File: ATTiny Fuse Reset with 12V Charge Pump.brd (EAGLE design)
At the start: 59 parts, among them IC1 74HC04D, Q1 BSS138, Q2 PMV65XP, Q3 BSS138, Q4 BSS138, Q5 BSS138, Q6 BSS138, Q7 BSS138, Q8 BSS130, SW3 SWITCH_SPDT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

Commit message: added dimnsion layer
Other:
- board outline added: 68.6 x 53.3 mm
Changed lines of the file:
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@@
 <grid distance="50" unitdist="mil" unit="mil" style="lines" multiple="5" display="yes" altdistance="5" altunitdist="mil" altunit="mil"/>
 <layers>
-<layer number="1" name="Top" color="4" fill="1" visible="yes" active="yes"/>
+<layer number="1" name="Top" color="4" fill="1" visible="no" active="yes"/>
 <layer number="16" name="Bottom" color="1" fill="1" visible="yes" active="yes"/>
-<layer number="17" name="Pads" color="2" fill="1" visible="yes" active="yes"/>
-<layer number="18" name="Vias" color="2" fill="1" visible="yes" active="yes"/>
-<layer number="19" name="Unrouted" color="6" fill="1" visible="yes" active="yes"/>
+<layer number="17" name="Pads" color="2" fill="1" visible="no" active="yes"/>
+<layer number="18" name="Vias" color="2" fill="1" visible="no" active="yes"/>
+<layer number="19" name="Unrouted" color="6" fill="1" visible="no" active="yes"/>
 <layer number="20" name="Dimension" color="15" fill="1" visible="yes" active="yes"/>
-<layer number="21" name="tPlace" color="16" fill="1" visible="yes" active="yes"/>
+<layer number="21" name="tPlace" color="16" fill="1" visible="no" active="yes"/>
 <layer number="22" name="bPlace" color="14" fill="1" visible="yes" active="yes"/>
-<layer number="23" name="tOrigins" color="15" fill="1" visible="yes" active="yes"/>
-<layer number="24" name="bOrigins" color="15" fill="1" visible="yes" active="yes"/>
+<layer number="23" name="tOrigins" color="15" fill="1" visible="no" active="yes"/>
+<layer number="24" name="bOrigins" color="15" fill="1" visible="no" active="yes"/>
 <layer number="25" name="tNames" color="7" fill="1" visible="no" active="yes"/>
 <layer number="26" name="bNames" color="7" fill="1" visible="no" active="yes"/>
@@
 <layer number="32" name="bCream" color="7" fill="5" visible="no" active="yes"/>
 <layer number="44" name="Drills" color="7" fill="1" visible="no" active="yes"/>
-<layer number="45" name="Holes" color="7" fill="1" visible="yes" active="yes"/>
+<layer number="45" name="Holes" color="7" fill="1" visible="no" active="yes"/>
 <layer number="50" name="dxf" color="7" fill="1" visible="no" active="no"/>
-<layer number="51" name="tDocu" color="6" fill="1" visible="yes" active="yes"/>
+<layer number="51" name="tDocu" color="6" fill="1" visible="no" active="yes"/>
 <layer number="52" name="bDocu" color="7" fill="1" visible="no" active="yes"/>
 <layer number="53" name="tGND_GNDA" color="7" fill="9" visible="no" active="no"/>
@@
 HV / ISP
 Programmer</text>
+<wire x1="0" y1="53.34" x2="0" y2="0" width="0.000253125" layer="20"/>
+<wire x1="0" y1="0" x2="66.04" y2="0" width="0.000253125" layer="20"/>
+<wire x1="66.04" y1="0" x2="66.04" y2="2.54" width="0.000253125" layer="20"/>
+<wire x1="66.04" y1="2.54" x2="68.58" y2="5.08" width="0.000253125" layer="20"/>
+<wire x1="68.58" y1="5.08" x2="68.58" y2="37.846" width="0.000253125" layer="20"/>
+<wire x1="68.58" y1="37.846" x2="66.04" y2="40.386" width="0.000253125" layer="20"/>
+<wire x1="66.04" y1="40.386" x2="66.04" y2="51.816" width="0.000253125" layer="20"/>
+<wire x1="66.04" y1="51.816" x2="64.516" y2="53.34" width="0.000253125" layer="20"/>
+<wire x1="64.516" y1="53.34" x2="0" y2="53.34" width="0.000253125" layer="20"/>
 </plain>
 <attributes>

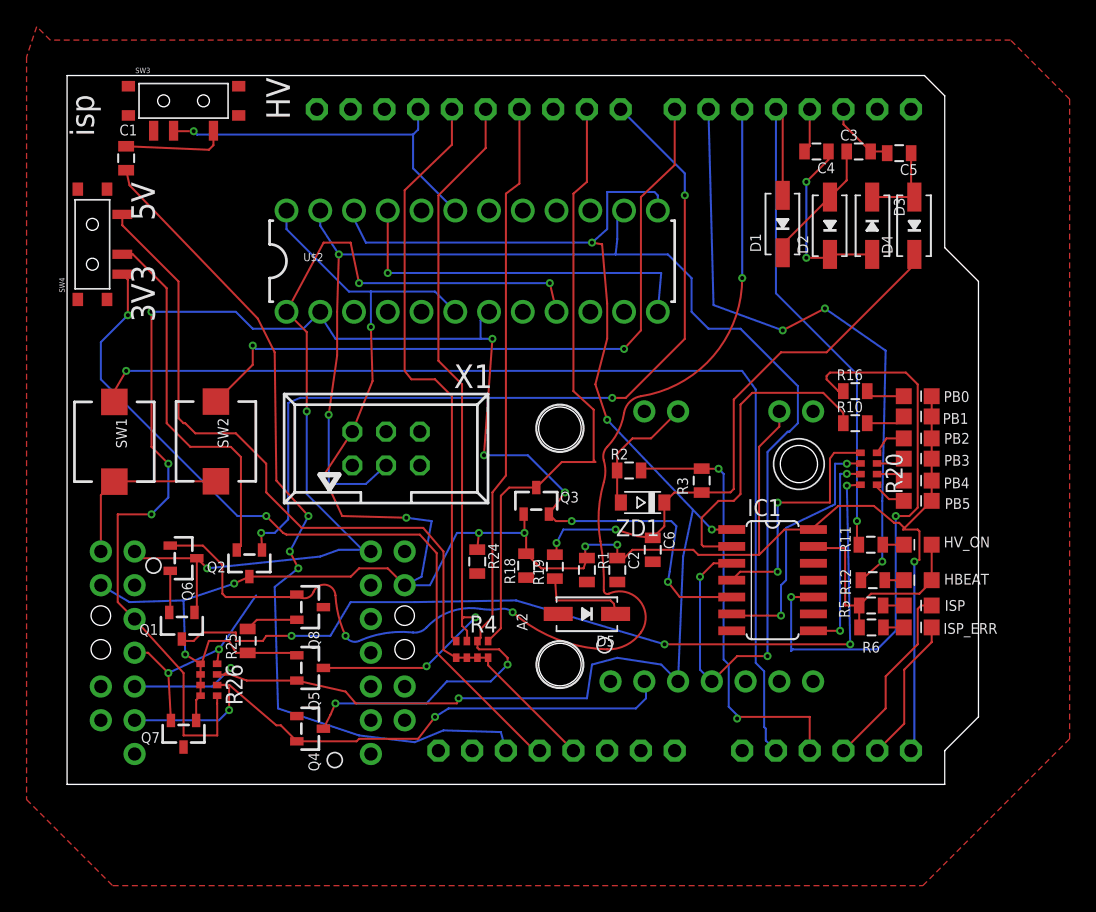
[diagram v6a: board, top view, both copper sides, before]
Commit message: aligned xtra pins overlayed on attami device
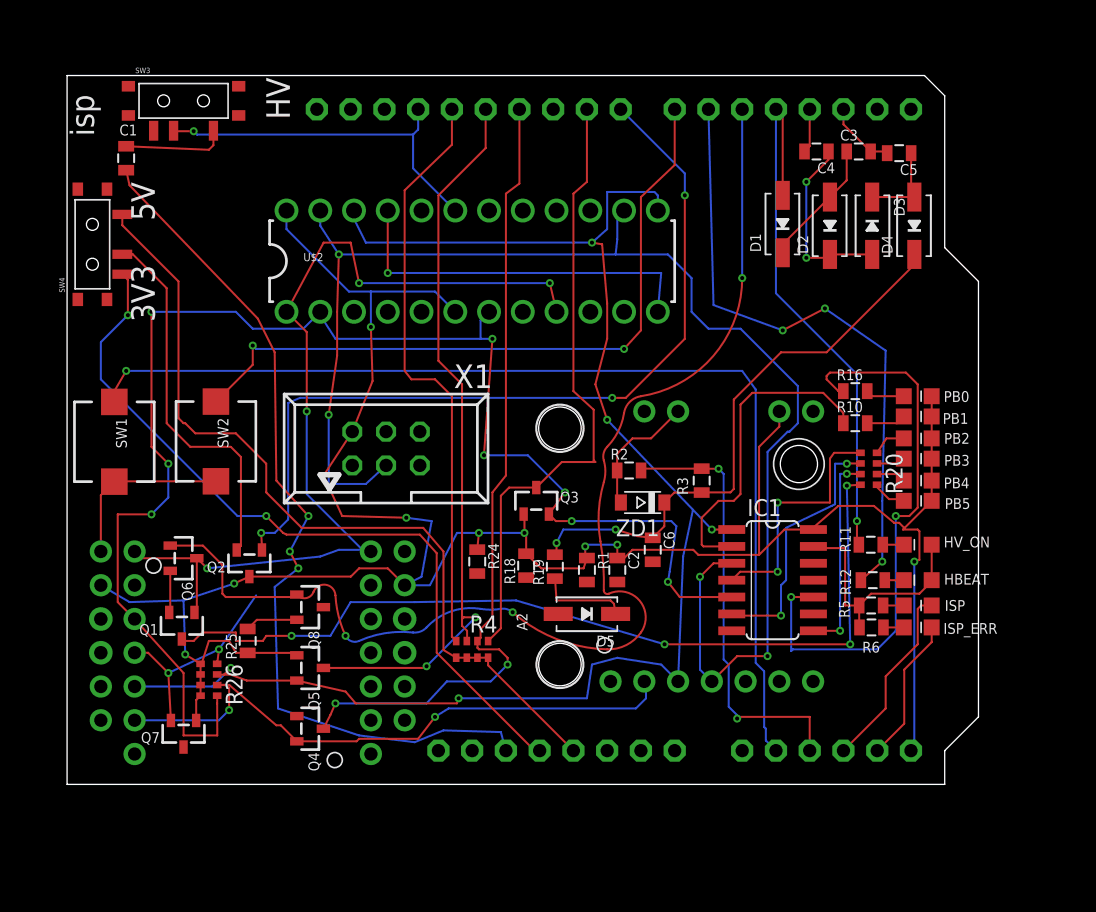
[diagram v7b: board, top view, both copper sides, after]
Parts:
- added JP3, JP4: (no value), ATtami:1X01-CLEANBIG
- JP1, JP2: value M02POGO_PIN_HOLES_ONLY -> (none); device SparkFun-Connectors:1X02_PP_HOLES_ONLY -> ATtami:1X01-CLEANBIG
- moved JP1 0.25 mm to (25.4, 9.91)
- moved JP2 0.25 mm to (2.54, 9.91)
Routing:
- removed copper zone on layer 1, net GND

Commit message: topoR first effort, not bad
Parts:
- A1: value ATTami -> (none)
- C1: value 10uF -> (none)
- C2, C6: value 2uF -> (none)
- C3, C4, C5: value 0.2uF -> (none)
- D1, D2, D3, D5: value 1N4148 -> (none)
- R11, R12, R5, R6: value 220R -> (none)
- R19: value 2.2K -> (none)
- R2: value 100K -> (none)
- R24: value 1k -> (none)
- R3: value 510K -> (none)
- U1: value ARDUINOR3-BPLACE -> (none)
- ZD1: value 12V_zener -> (none)
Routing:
- net GND: track 76.2 -> 234.5 mm, vias 1 -> 7
- net N$3: track 0.00 -> 72.9 mm, vias 0 -> 1
- net SDI_MOSI: track 74.9 -> 104.3 mm
- net N$13: track 43.4 -> 16.7 mm
- net ISP_RESET: track 0.00 -> 26.2 mm, vias 0 -> 2
- net HV_OFF(RESET): track 86.2 -> 64.1 mm, vias 3 -> 4
- net N$34: track 44.1 -> 65.4 mm, vias 0 -> 4
- net N$9: track 78.5 -> 59.1 mm, vias 1 -> 2
- net HV/RESET: track 78.3 -> 96.0 mm
- net SCI: track 110.8 -> 94.6 mm, vias 8 -> 5
- net ATTINY_VCC: track 181.2 -> 166.8 mm
- net VCC_OFF: track 63.5 -> 49.5 mm, vias 3 -> 2
- net N$33: track 65.8 -> 54.9 mm, vias 3 -> 2
- net N$21: track 24.2 -> 14.3 mm
- net SII-MISO: track 116.1 -> 106.3 mm, vias 5 -> 4
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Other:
- board text added: "|&lt;--14 pin--&gt;|"
- board text added: "|&lt;8 pin&gt;|"
- board text removed: "|<--14 pin-->|"
- board text removed: "|<8 pin>|"
